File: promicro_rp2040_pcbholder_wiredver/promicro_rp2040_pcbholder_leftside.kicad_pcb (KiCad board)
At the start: 2 copper layers, 34.3 x 38.3 mm, 7 parts, among them J3 Conn_01x08_Pin, J4 Conn_01x08_Pin, U3 RP2040_Pro_Micro, U4 TRRS

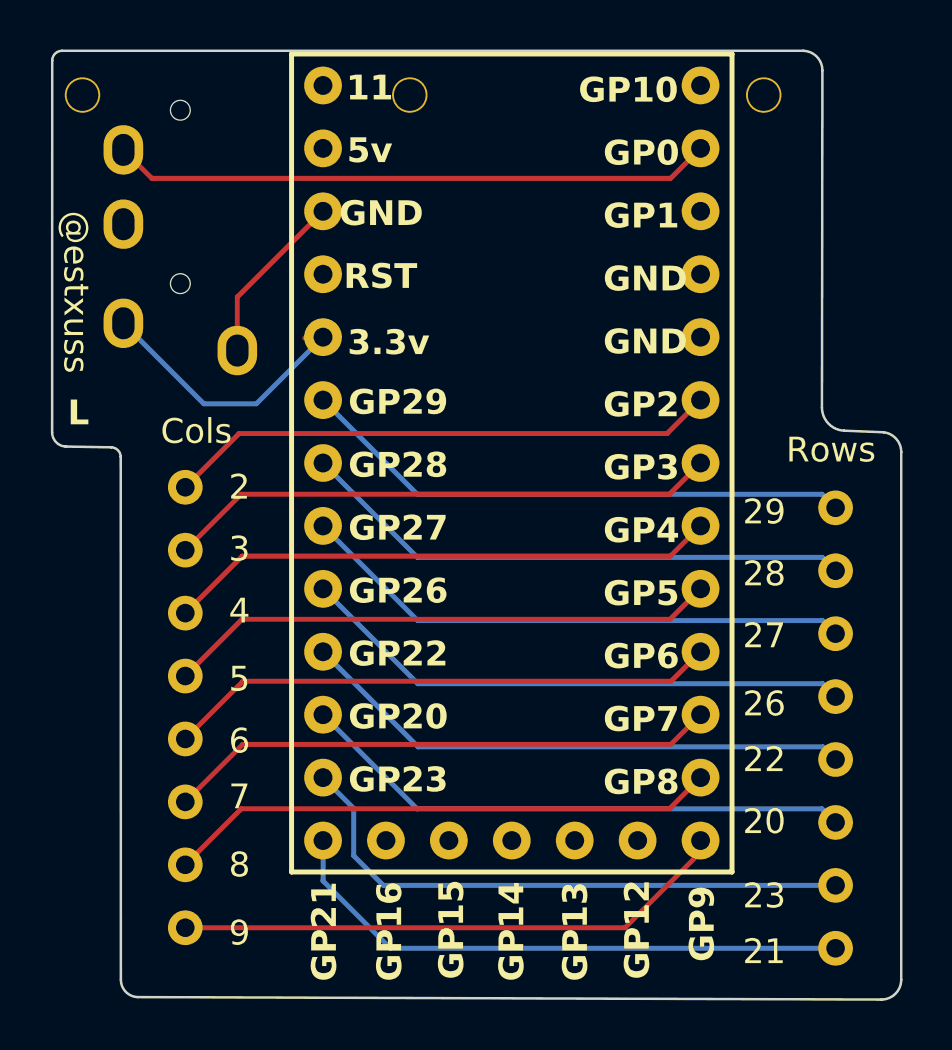
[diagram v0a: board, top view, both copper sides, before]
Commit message: tested working. Swap left side pcb's rows and cols wire holes
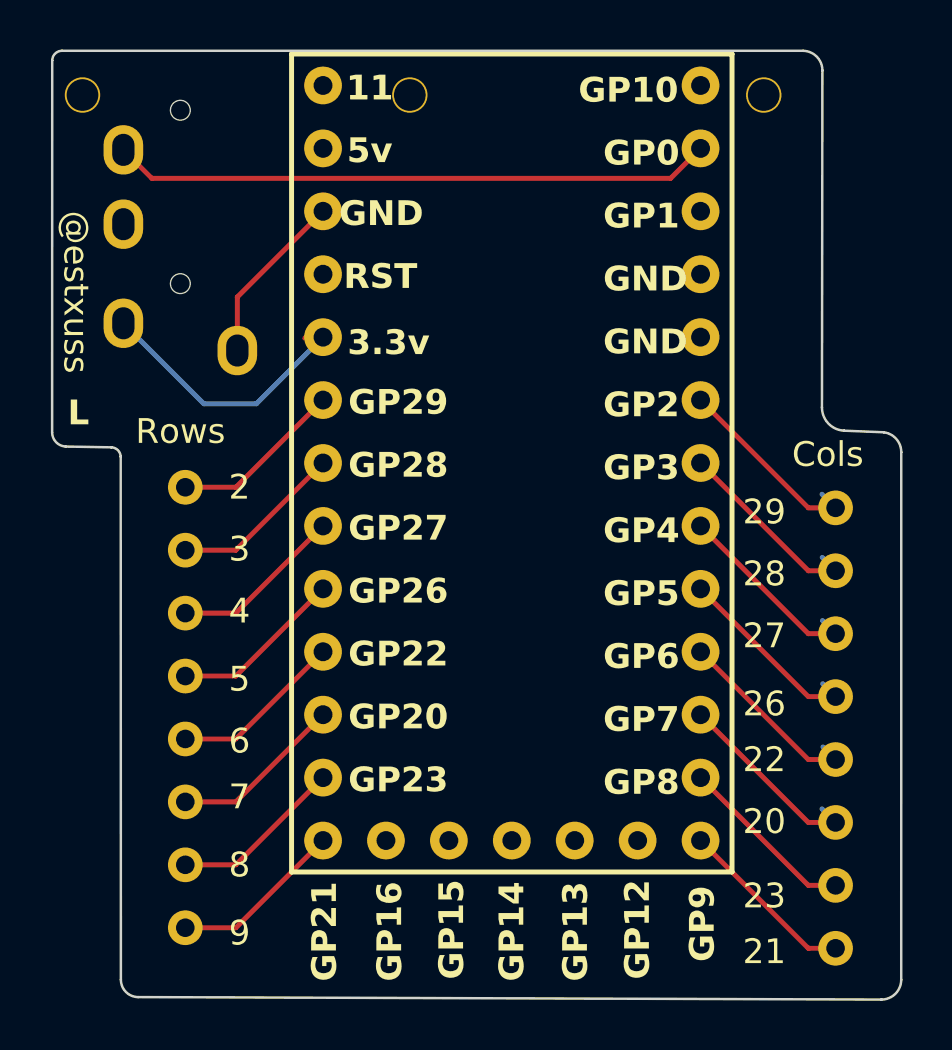
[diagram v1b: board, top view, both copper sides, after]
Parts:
- moved J3 26.3 mm to (163.0, 38.5)
- moved J4 26.3 mm to (136.7, 37.6)
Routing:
- net LRow7: track 23.6 -> 7.02 mm
- net LRow8: track 23.4 -> 7.02 mm
- net LRow2: track 22.5 -> 7.02 mm
- net LRow5: track 22.5 -> 7.02 mm
- net LRow4: track 22.5 -> 7.02 mm
- net LRow3: track 22.5 -> 7.02 mm
- net LRow1: track 22.5 -> 7.02 mm
- net LRow6: track 22.5 -> 7.02 mm
- net LCol7: track 22.3 -> 7.25 mm
- net LCol8: track 22.5 -> 7.72 mm
- net LCol5: track 22.3 -> 7.97 mm
- net LCol4: track 22.3 -> 7.99 mm
- net LCol3: track 22.3 -> 8.00 mm
- net LCol2: track 22.3 -> 8.02 mm
- net LCol1: track 22.3 -> 8.03 mm
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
